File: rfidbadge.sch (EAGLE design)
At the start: 2 parts, among them U1 ATMEGA328P_TQFP, U2 CLRC663

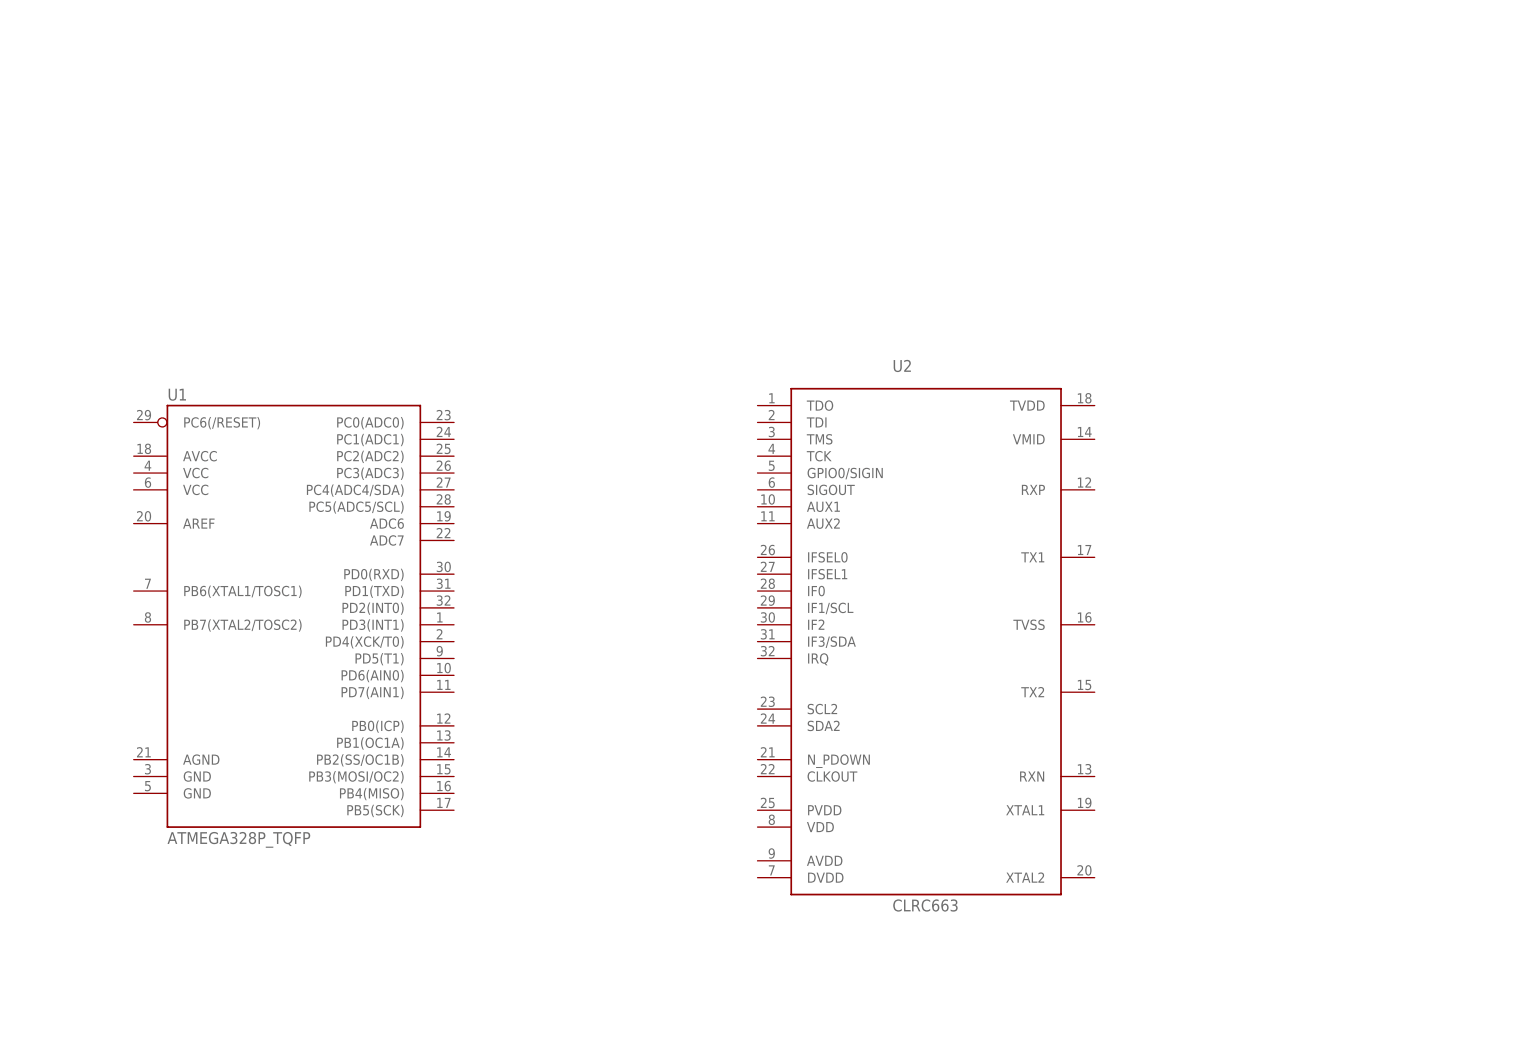
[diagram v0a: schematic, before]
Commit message: Wired up power and a crystal
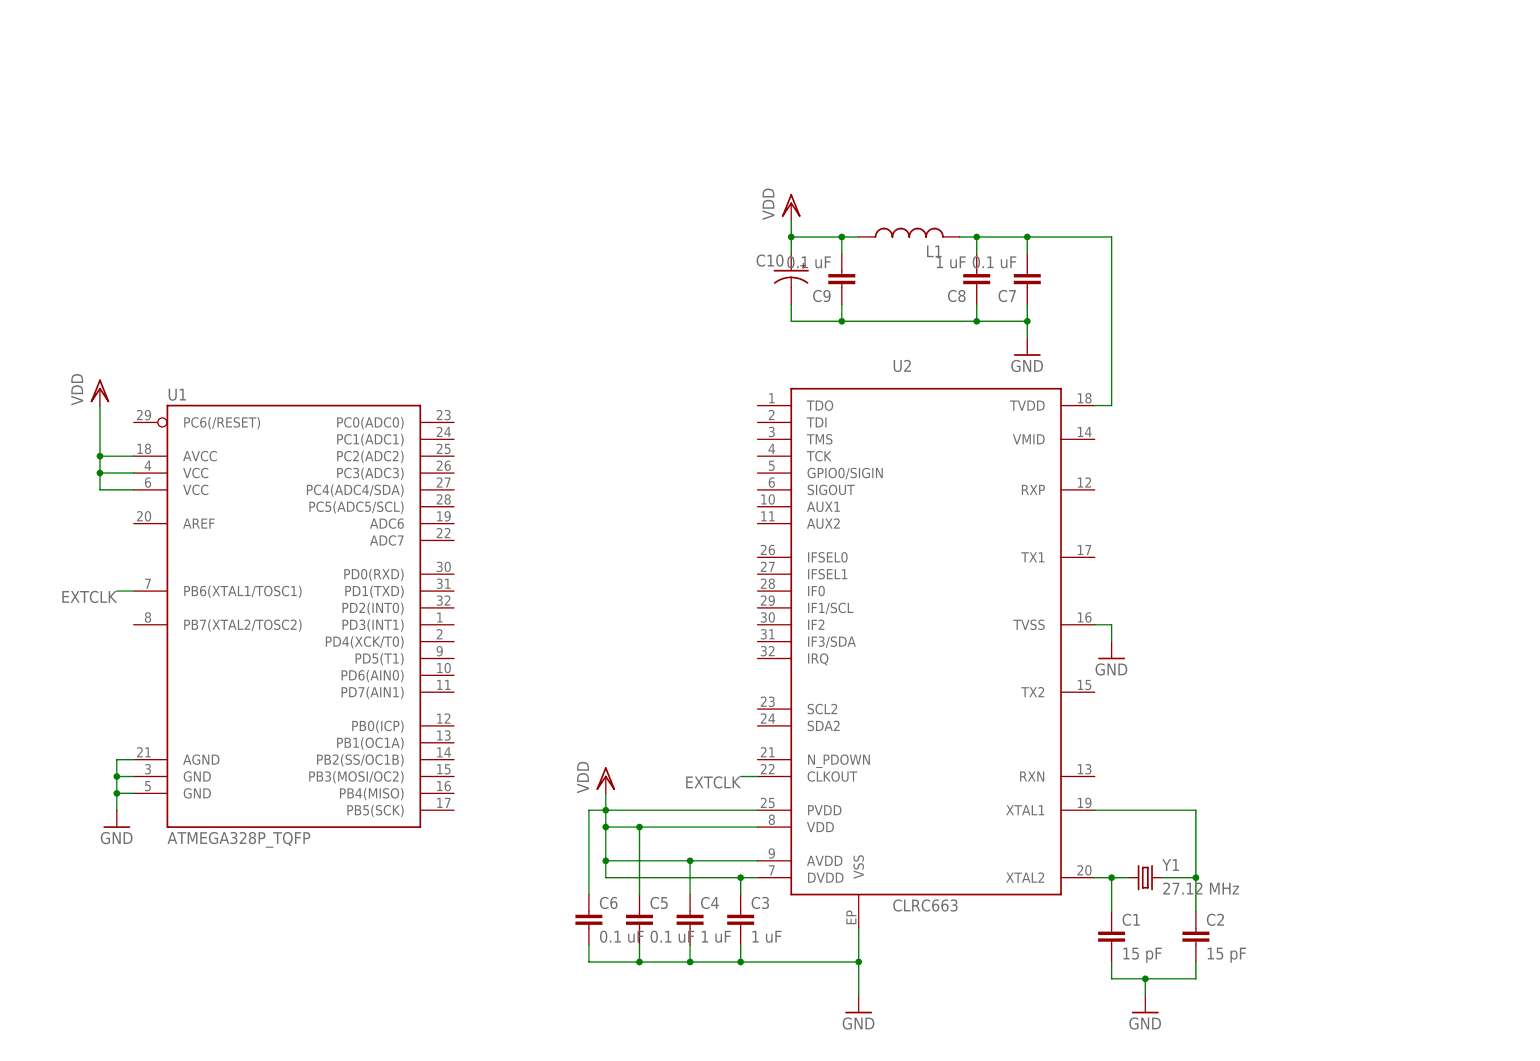
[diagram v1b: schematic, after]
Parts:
- added C1, C2: 15 pF, rcl:C-EUC0603K
- added C10: (no value), rcl:CPOL-US085CS-1AR
- added C3, C4, C8: 1 uF, rcl:C-EUC0603K
- added C5, C6, C7, C9: 0.1 uF, rcl:C-EUC0603K
- added L1: (no value), rcl:L-USL0201
- added Y1: 27.12 MHz, SparkFun-FreqCtrl:CRYSTALCRYSTAL-SMD-5X3-12.288MHZ
- U1: PROD_ID (none) -> ATMEGA328PB-AURCT-ND
- U2: PROD_ID (none) -> 568-11528-ND
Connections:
- new net EXTCLK: U1.PB6(XTAL1/TOSC1), U2.CLKOUT
- new net GND: C1.2, C10.-, C2.2, C3.2, C4.2, C5.2, C6.2, C7.1, C8.1, C9.1, U1.AGND, U1.GND@3, U1.GND@5, U2.TVSS, U2.VSS
- new net N$1: C1.1, U2.XTAL2, Y1.1
- new net N$2: C2.1, U2.XTAL1, Y1.2
- new net N$8: C7.2, C8.2, L1.2, U2.TVDD
- new net VDD: C10.+, C3.1, C4.1, C5.1, C6.1, C9.2, L1.1, U1.AVCC, U1.VCC@4, U1.VCC@6, U2.AVDD, U2.DVDD, U2.PVDD, U2.VDD

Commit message: Added display and wired up I2C
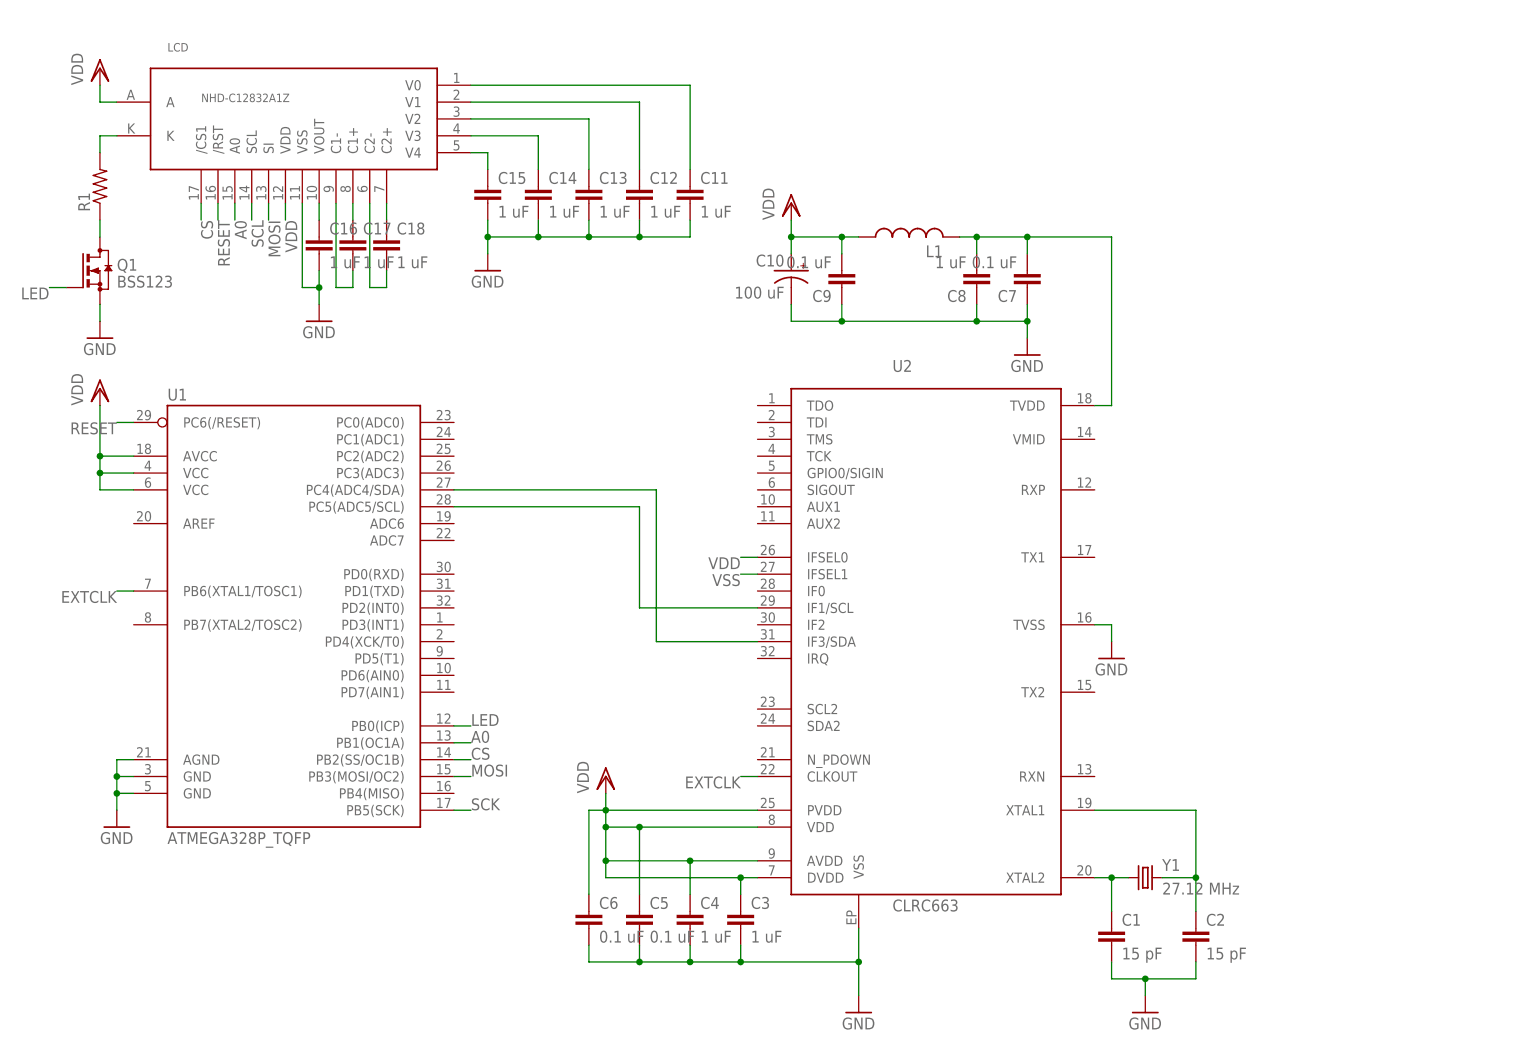
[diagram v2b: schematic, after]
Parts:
- added C11, C12, C13, C14, C15, C16, C17, C18: 1 uF, rcl:C-EUC0603K
- added LCD: NHD-C12832A1Z, display:NHD-C12832A1Z
- added Q1: BSS123, transistor-small-signal:BSS123
- added R1: (no value), rcl:R-US_R0603
- C10: value (none) -> 100 uF
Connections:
- new net A0: LCD.A0, U1.PB1(OC1A)
- new net CS: LCD./CS1, U1.PB2(SS/OC1B)
- new net LED: Q1.G, U1.PB0(ICP)
- new net MOSI: LCD.SI, U1.PB3(MOSI/OC2)
- new net N$10: C11.1, LCD.V0
- new net N$11: C18.1, LCD.C2+
- new net N$12: C18.2, LCD.C2-
- new net N$13: C17.1, LCD.C1+
- new net N$14: C17.2, LCD.C1-
- new net N$15: C16.1, LCD.VOUT
- new net N$16: LCD.K, R1.2
- new net N$17: Q1.D, R1.1
- new net N$3: C15.1, LCD.V4
- new net N$4: U1.PC4(ADC4/SDA), U2.IF3/SDA
- new net N$5: U1.PC5(ADC5/SCL), U2.IF1/SCL
- new net N$6: C14.1, LCD.V3
- new net N$7: C13.1, LCD.V2
- new net N$9: C12.1, LCD.V1
- new net RESET: LCD./RST, U1.PC6(/RESET)
- new net SCK: U1.PB5(SCK)
- new net SCL: LCD.SCL
- new net VSS: U2.IFSEL1
- net GND: now also C11.2, C12.2, C13.2, C14.2, C15.2, C16.2, LCD.VSS, Q1.S
- net VDD: now also LCD.A, LCD.VDD, U2.IFSEL0
